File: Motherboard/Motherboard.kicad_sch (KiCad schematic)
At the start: 53 parts, among them J1 Conn_01x01, J10 ATX-24, J11 USB_B, J12 Bus_ISA_8bit, J13 65SIB_Connector, J2 Conn_01x01, J3 Conn_01x01, J4 Conn_01x01, J5 Conn_01x01, J6 Conn_01x01, J7 Conn_01x01, J8 Conn_01x01, J9 Bus_ISA_8bit, SW1 SW_Push, SW2 SW_SPST, U1 SC28L91, U10 XCR3064XL-VQ100, U11 XCR3064-VQ100, U12 LM7905_TO220, U13 MCP2200-I-SO, U14 74HCT163, U15 74HCT137, U2 AS6C1608, U3 WD65C22, U4 SST39SF040, U5 SST39SF040, U6 WD65C816S, U7 DS1813, U8 74HCT245, U9 74HCT573, X1 ACO-3.6864MHz, X2 ACO-24MHz, X3 ACO-14.31818MHz

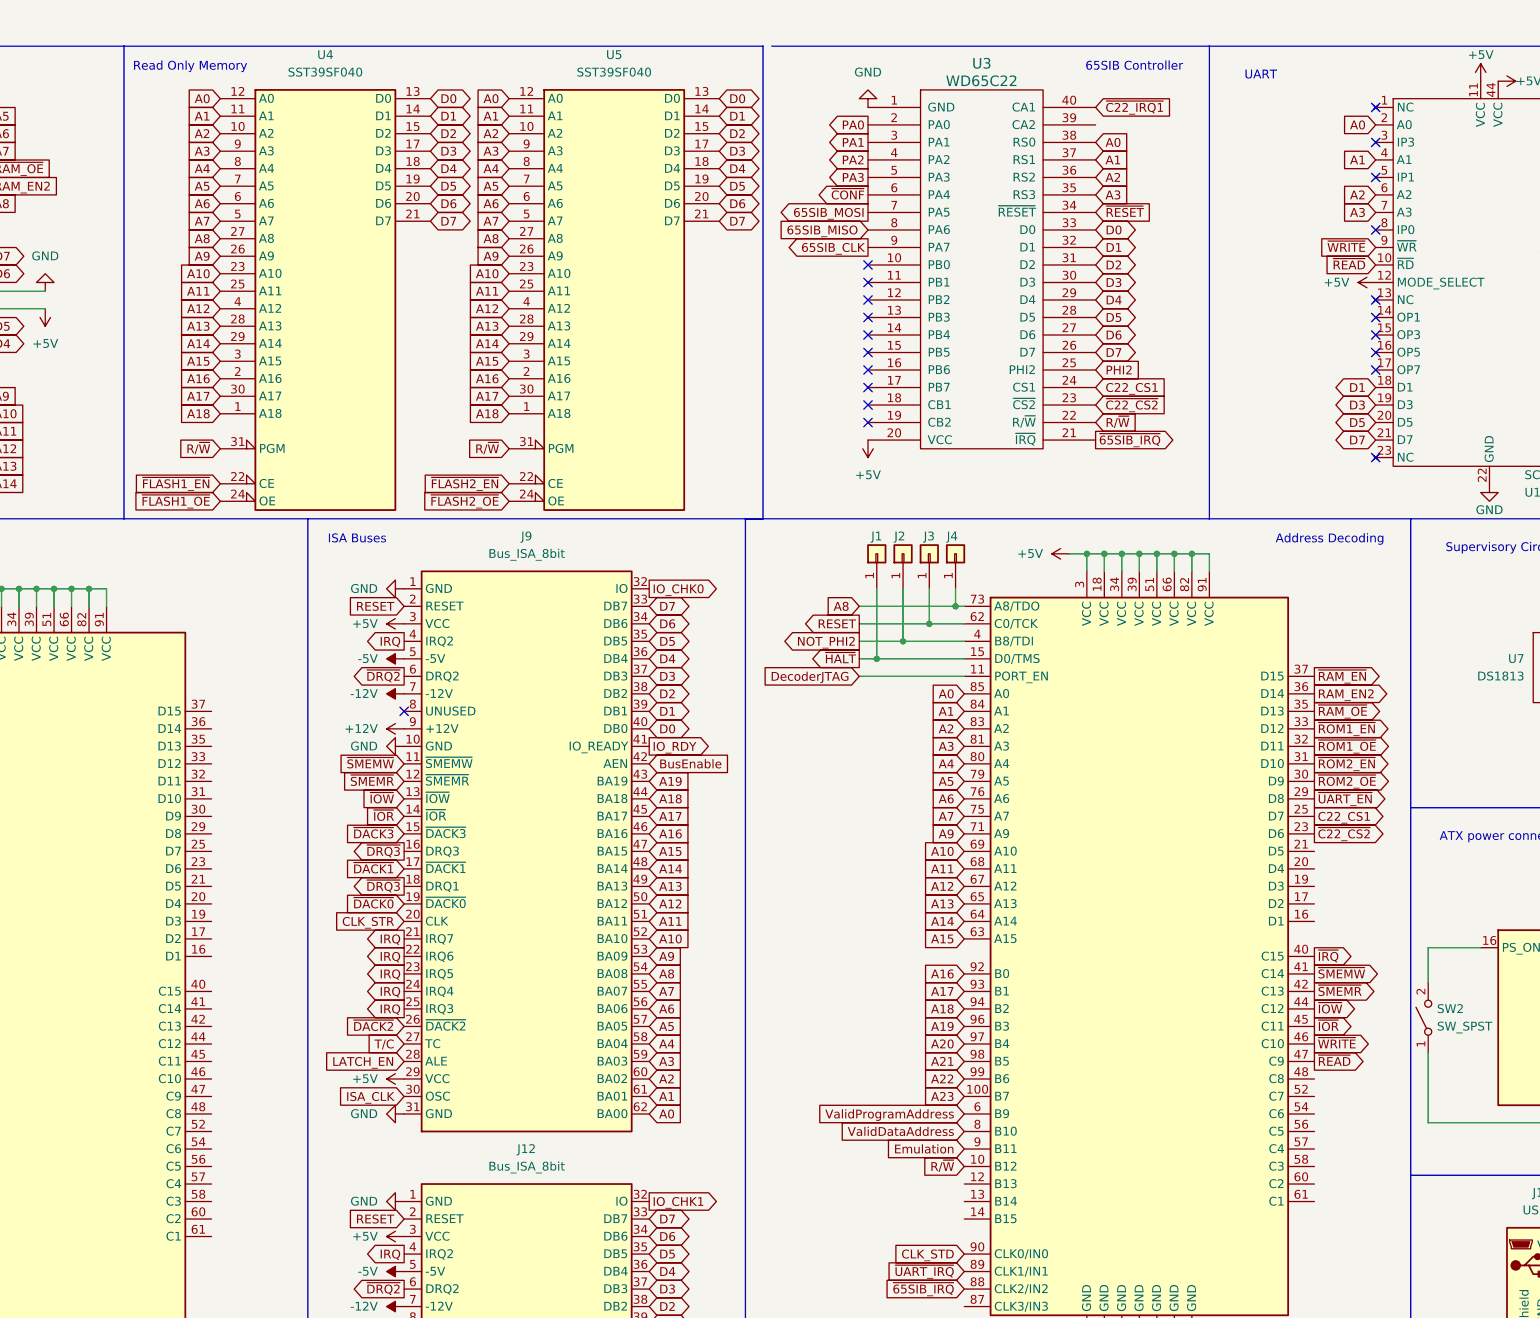
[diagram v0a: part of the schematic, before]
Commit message: Migrated files to Motherboard subfolder...
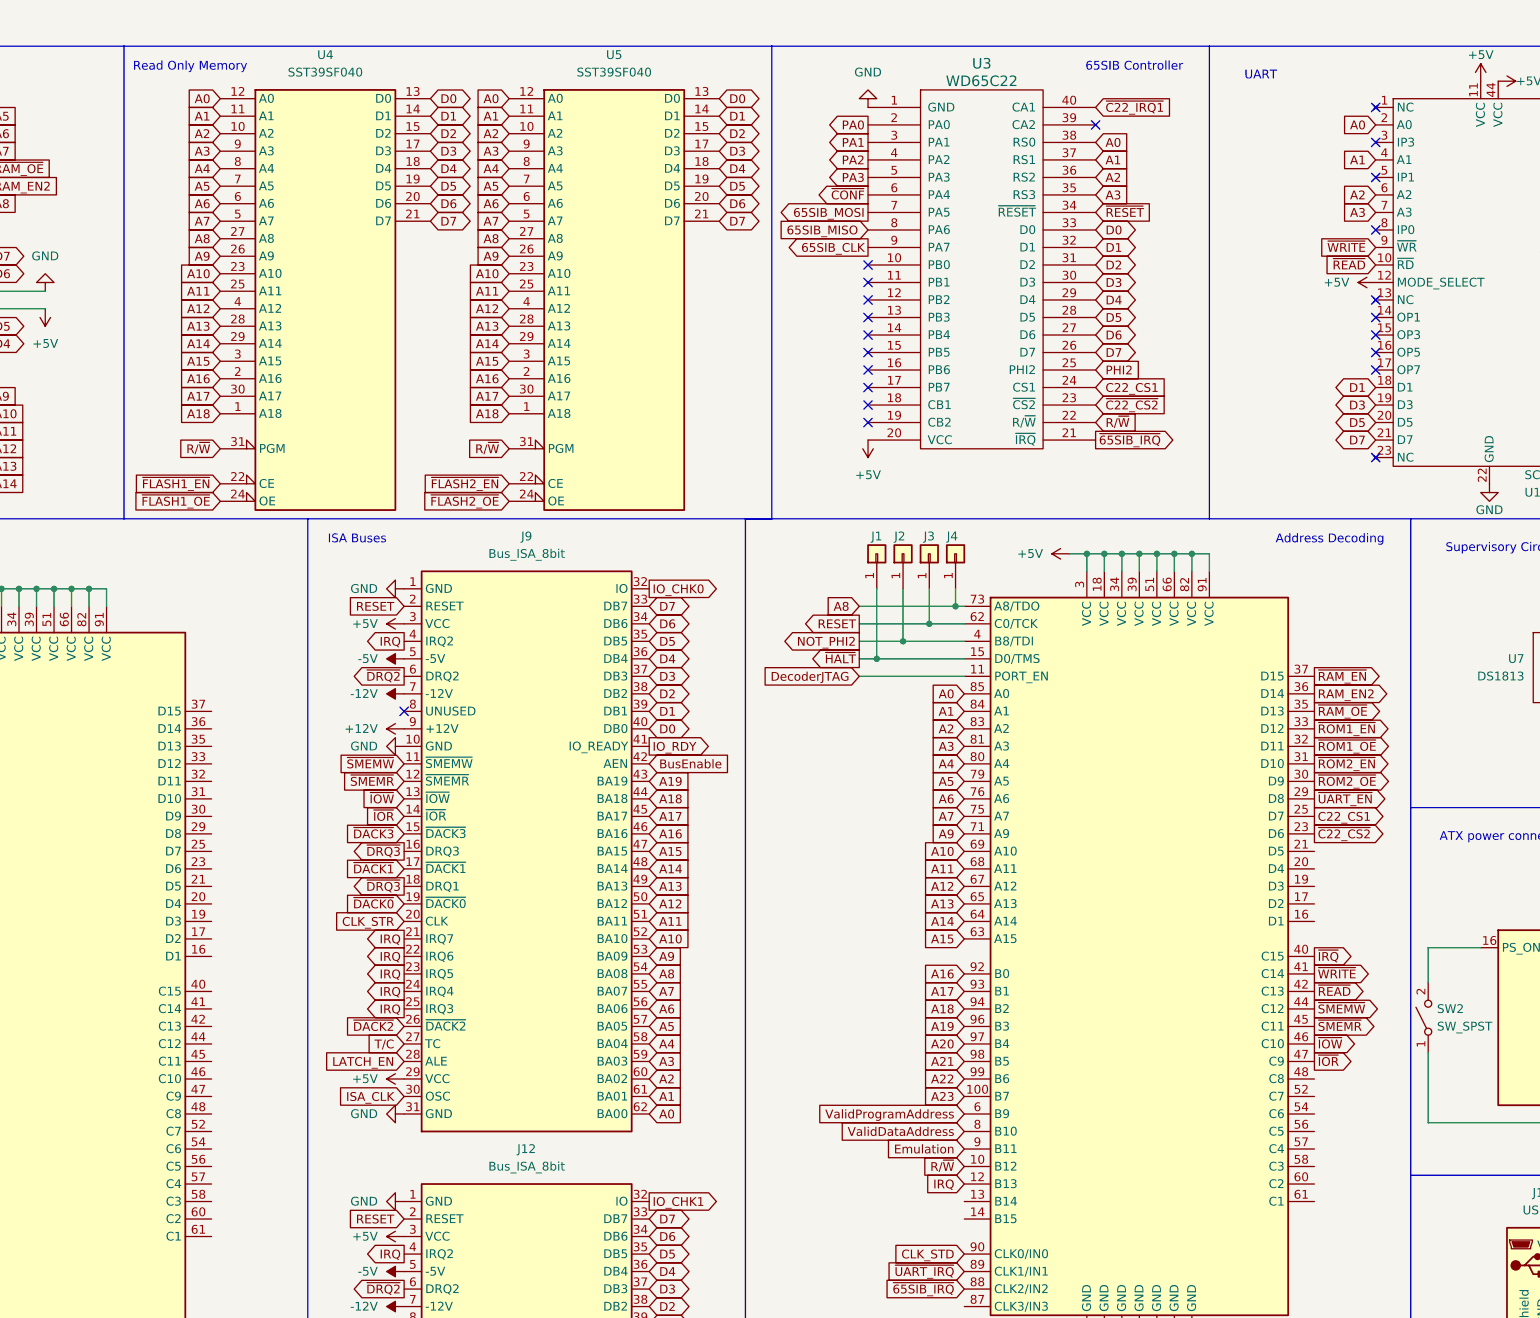
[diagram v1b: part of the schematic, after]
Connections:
- net IRQ: now also U10.12 (B13)
- net ~{IOR}: now also U10.47 (C9); no longer U10.45 (C11)
- net ~{IOW}: now also U10.46 (C10); no longer U10.44 (C12)
- net ~{READ}: now also U10.42 (C13); no longer U10.47 (C9)
- net ~{SMEMR}: now also U10.45 (C11); no longer U10.42 (C13)
- net ~{SMEMW}: now also U10.44 (C12); no longer U10.41 (C14)
- net ~{WRITE}: now also U10.41 (C14); no longer U10.46 (C10)
- no-connect marks 54 -> 55
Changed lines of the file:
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@@
   (no_connect (at 386.08 158.75))
   (no_connect (at 287.02 254))
+  (no_connect (at 304.8 26.67))
   (no_connect (at 204.47 111.76))
   (no_connect (at 204.47 200.66))
@@
     (stroke (width 0) (type default) (color 0 0 0 0))
   )
-  (polyline (pts (xy 256.54 83.82) (xy 256.54 15.24))
+  (polyline (pts (xy 257.81 83.82) (xy 257.81 15.24))
     (stroke (width 0) (type default) (color 0 0 0 0))
   )
@@
     (stroke (width 0) (type default) (color 0 0 0 0))
   )
-  (polyline (pts (xy 256.54 15.24) (xy 163.83 15.24))
+  (polyline (pts (xy 257.81 15.24) (xy 163.83 15.24))
     (stroke (width 0) (type default) (color 0 0 0 0))
   )
@@
     (stroke (width 0) (type default) (color 0 0 0 0))
   )
-  (polyline (pts (xy 163.83 83.82) (xy 256.54 83.82))
+  (polyline (pts (xy 163.83 83.82) (xy 257.81 83.82))
     (stroke (width 0) (type default) (color 0 0 0 0))
   )
@@
     )
   )
+  (global_label "IRQ" (shape input) (at 285.75 180.34 180) (fields_autoplaced)
+    (effects (font (size 1.27 1.27)) (justify right))
+    (property "Intersheet References" "${INTERSHEET_REFS}" (id 0) (at 280.1317 180.2606 0)
+      (effects (font (size 1.27 1.27)) (justify right) hide)
+    )
+  )
   (global_label "RESET" (shape input) (at 204.47 185.42 180) (fields_autoplaced)
     (effects (font (size 1.27 1.27)) (justify right))
@@
     )
   )
-  (global_label "~{WRITE}" (shape output) (at 336.55 160.02 0) (fields_autoplaced)
-    (effects (font (size 1.27 1.27)) (justify left))
-    (property "Intersheet References" "${INTERSHEET_REFS}" (id 0) (at 344.406 159.9406 0)
+  (global_label "~{WRITE}" (shape output) (at 336.55 149.86 0) (fields_autoplaced)
+    (effects (font (size 1.27 1.27)) (justify left))
+    (property "Intersheet References" "${INTERSHEET_REFS}" (id 0) (at 344.406 149.7806 0)
       (effects (font (size 1.27 1.27)) (justify left) hide)
     )
@@
     )
   )
-  (global_label "~{IOW}" (shape output) (at 336.55 154.94 0) (fields_autoplaced)
-    (effects (font (size 1.27 1.27)) (justify left))
-    (property "Intersheet References" "${INTERSHEET_REFS}" (id 0) (at 342.3498 154.8606 0)
+  (global_label "~{IOW}" (shape output) (at 336.55 160.02 0) (fields_autoplaced)
+    (effects (font (size 1.27 1.27)) (justify left))
+    (property "Intersheet References" "${INTERSHEET_REFS}" (id 0) (at 342.3498 159.9406 0)
       (effects (font (size 1.27 1.27)) (justify left) hide)
     )
@@
     )
   )
-  (global_label "~{SMEMW}" (shape output) (at 336.55 149.86 0) (fields_autoplaced)
-    (effects (font (size 1.27 1.27)) (justify left))
-    (property "Intersheet References" "${INTERSHEET_REFS}" (id 0) (at 345.676 149.7806 0)
+  (global_label "~{SMEMW}" (shape output) (at 336.55 154.94 0) (fields_autoplaced)
+    (effects (font (size 1.27 1.27)) (justify left))
+    (property "Intersheet References" "${INTERSHEET_REFS}" (id 0) (at 345.676 154.8606 0)
       (effects (font (size 1.27 1.27)) (justify left) hide)
     )
@@
     )
   )
-  (global_label "~{READ}" (shape output) (at 336.55 162.56 0) (fields_autoplaced)
-    (effects (font (size 1.27 1.27)) (justify left))
-    (property "Intersheet References" "${INTERSHEET_REFS}" (id 0) (at 343.7407 162.4806 0)
+  (global_label "~{READ}" (shape output) (at 336.55 152.4 0) (fields_autoplaced)
+    (effects (font (size 1.27 1.27)) (justify left))
+    (property "Intersheet References" "${INTERSHEET_REFS}" (id 0) (at 343.7407 152.3206 0)
       (effects (font (size 1.27 1.27)) (justify left) hide)
     )
@@
     )
   )
-  (global_label "~{SMEMR}" (shape output) (at 336.55 152.4 0) (fields_autoplaced)
-    (effects (font (size 1.27 1.27)) (justify left))
-    (property "Intersheet References" "${INTERSHEET_REFS}" (id 0) (at 345.4945 152.3206 0)
+  (global_label "~{SMEMR}" (shape output) (at 336.55 157.48 0) (fields_autoplaced)
+    (effects (font (size 1.27 1.27)) (justify left))
+    (property "Intersheet References" "${INTERSHEET_REFS}" (id 0) (at 345.4945 157.4006 0)
       (effects (font (size 1.27 1.27)) (justify left) hide)
     )
@@
     )
   )
-  (global_label "~{IOR}" (shape output) (at 336.55 157.48 0) (fields_autoplaced)
-    (effects (font (size 1.27 1.27)) (justify left))
-    (property "Intersheet References" "${INTERSHEET_REFS}" (id 0) (at 342.1683 157.4006 0)
-      (effects (font (size 1.27 1.27)) (justify left) hide)
-    )
+  (global_label "~{IOR}" (shape output) (at 336.55 162.56 0) (fields_autoplaced)
+    (effects (font (size 1.27 1.27)) (justify left))
+    (property "Intersheet References" "${INTERSHEET_REFS}" (id 0) (at 342.1683 162.4806 0)
+      (effects (font (size 1.27 1.27)) (justify left) hide)
+    )
